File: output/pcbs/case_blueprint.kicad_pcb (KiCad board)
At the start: 2 copper layers, 124.4 x 92.7 mm, 5 parts

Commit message: updated footprints to ceoloide footprints
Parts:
- moved _2 18.7 mm to (183.2, 73.4)
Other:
- net class Default added: clearance 0.2, trace_width 0.25, via_dia 0.8, via_drill 0.4

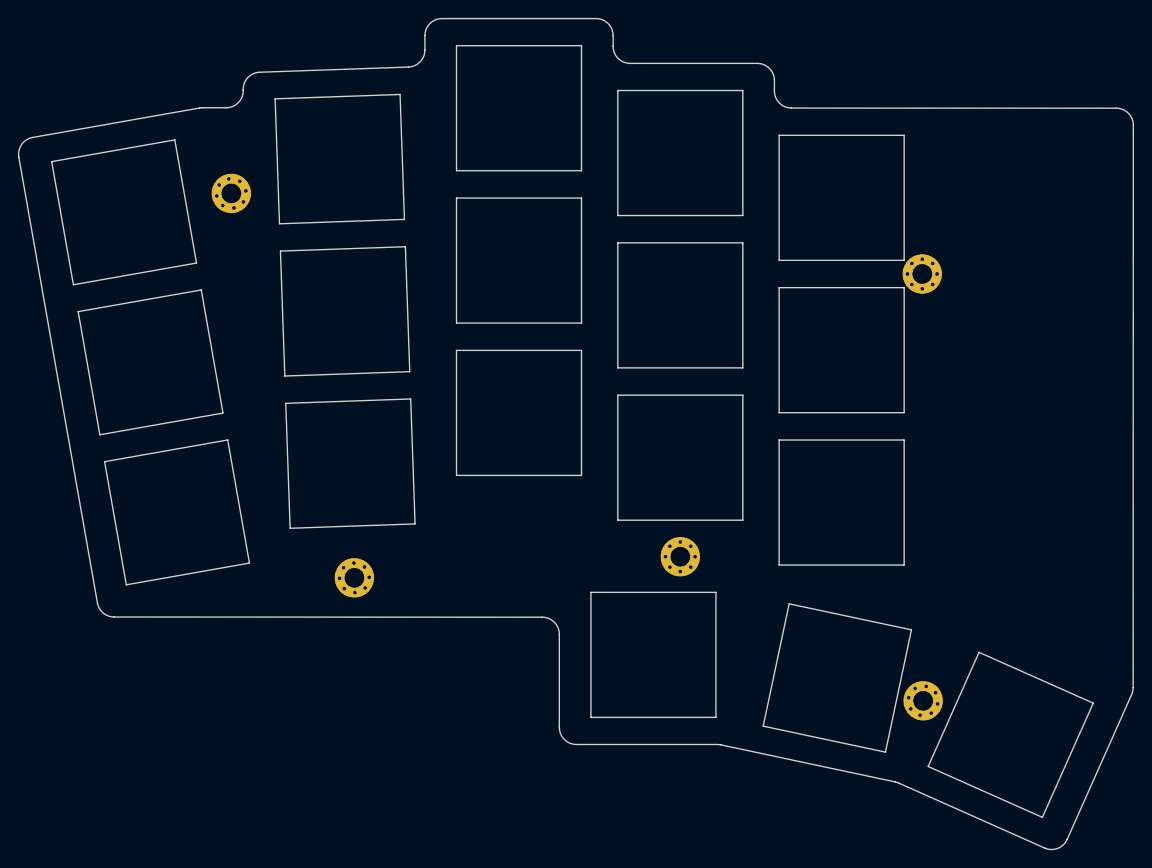
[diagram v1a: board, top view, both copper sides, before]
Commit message: redefined mounting holes positions
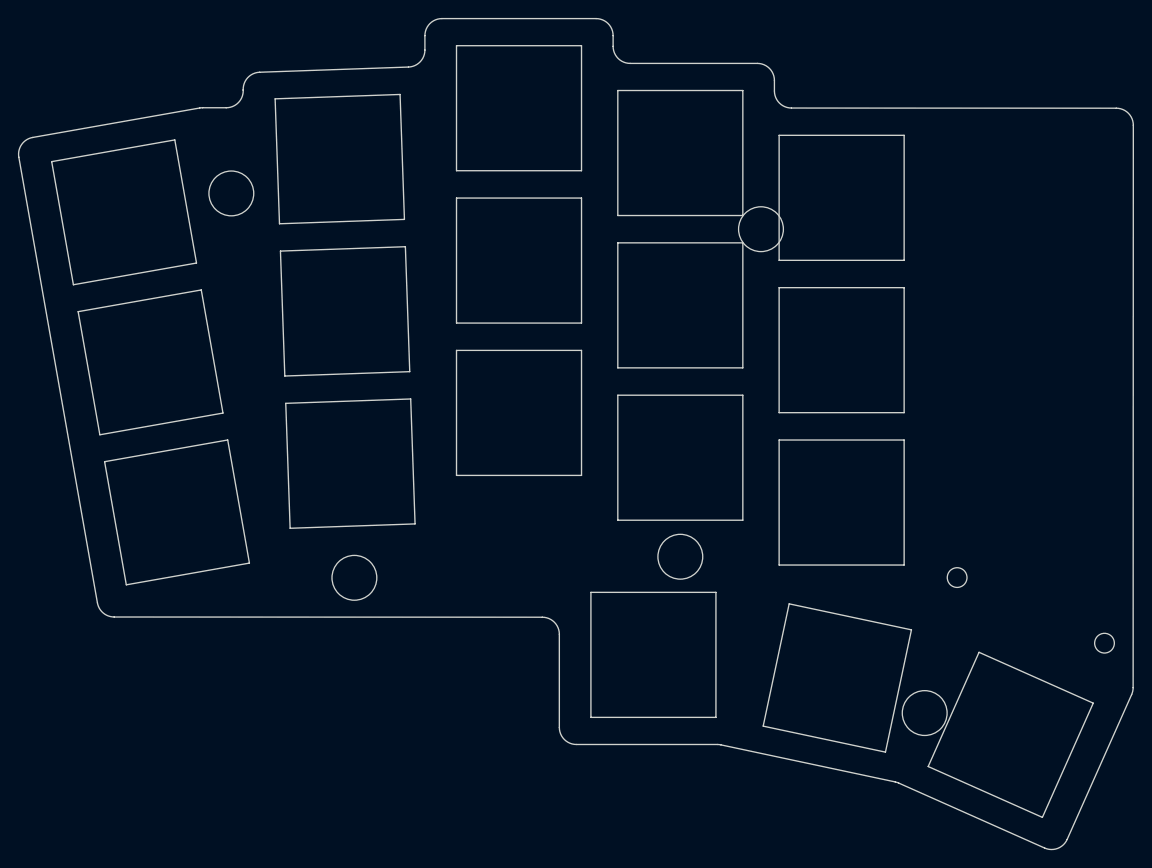
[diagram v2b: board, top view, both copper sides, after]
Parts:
- removed _1, _2, _3, _4, _5: , MountingHole_2.2mm_M2_Pad_Via
- added MH1: , ceoloide:mounting_hole_npth, F.Cu at (203.5, 114.6)
- added MH2: , ceoloide:mounting_hole_npth, F.Cu at (187.1, 107.3)
- added MH3: , ceoloide:mounting_hole_npth, F.Cu at (106.1, 64.4)
- added MH4: , ceoloide:mounting_hole_npth, F.Cu at (165.2, 68.4)
- added MH5: , ceoloide:mounting_hole_npth, F.Cu at (119.8, 107.3)
- added MH6: , ceoloide:mounting_hole_npth, F.Cu at (156.2, 104.9)
- added MH7: , ceoloide:mounting_hole_npth, F.Cu at (183.4, 122.4)
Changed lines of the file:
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@@
     (add_net "")
   )
-    (module "MountingHole_2.2mm_M2_Pad_Via" (version 20210722) (generator pcbnew) (layer "F.Cu")
-      (at 106.06137619999998 64.406711 10)
-      (fp_text reference "_1" (at 0 -3.2) (layer "F.SilkS") hide
-        (effects (font (size 1 1) (thickness 0.15)))
-      )
-      (fp_circle (center 0 0) (end 2.45 0) (layer "F.CrtYd") (width 0.05) (fill none))
-      (pad "1" thru_hole circle locked (at 1.166726 1.166726) (size 0.7 0.7) (drill 0.4) (layers *.Cu *.Mask))
-      (pad "1" thru_hole circle locked (at 0 0) (size 4.4 4.4) (drill 2.2) (layers *.Cu *.Mask))
-      (pad "1" thru_hole circle locked (at 0 1.65) (size 0.7 0.7) (drill 0.4) (layers *.Cu *.Mask))
-      (pad "1" thru_hole circle locked (at 1.166726 -1.166726) (size 0.7 0.7) (drill 0.4) (layers *.Cu *.Mask))
-      (pad "1" thru_hole circle locked (at -1.65 0) (size 0.7 0.7) (drill 0.4) (layers *.Cu *.Mask))
-      (pad "1" thru_hole circle locked (at -1.166726 -1.166726) (size 0.7 0.7) (drill 0.4) (layers *.Cu *.Mask))
-      (pad "1" thru_hole circle locked (at -1.166726 1.166726) (size 0.7 0.7) (drill 0.4) (layers *.Cu *.Mask))
-      (pad "1" thru_hole circle locked (at 1.65 0) (size 0.7 0.7) (drill 0.4) (layers *.Cu *.Mask))
-      (pad "1" thru_hole circle locked (at 0 -1.65) (size 0.7 0.7) (drill 0.4) (layers *.Cu *.Mask))
+  (footprint "ceoloide:mounting_hole_npth"
+    (layer "F.Cu")
+    (at 203.49527039999998 114.5930025 -24)
+    (property "Reference" "MH1"
+      (at 0 2.55 -24)
+      (layer "F.SilkS")
+      hide
+      (effects (font (size 1 1) (thickness 0.15)))
     )
-    (module "MountingHole_2.2mm_M2_Pad_Via" (version 20210722) (generator pcbnew) (layer "F.Cu")
-      (at 183.16278699999998 73.3973763 0)
-      (fp_text reference "_2" (at 0 -3.2) (layer "F.SilkS") hide
-        (effects (font (size 1 1) (thickness 0.15)))
-      )
-      (fp_circle (center 0 0) (end 2.45 0) (layer "F.CrtYd") (width 0.05) (fill none))
-      (pad "1" thru_hole circle locked (at 1.166726 1.166726) (size 0.7 0.7) (drill 0.4) (layers *.Cu *.Mask))
-      (pad "1" thru_hole circle locked (at 0 0) (size 4.4 4.4) (drill 2.2) (layers *.Cu *.Mask))
-      (pad "1" thru_hole circle locked (at 0 1.65) (size 0.7 0.7) (drill 0.4) (layers *.Cu *.Mask))
-      (pad "1" thru_hole circle locked (at 1.166726 -1.166726) (size 0.7 0.7) (drill 0.4) (layers *.Cu *.Mask))
-      (pad "1" thru_hole circle locked (at -1.65 0) (size 0.7 0.7) (drill 0.4) (layers *.Cu *.Mask))
-      (pad "1" thru_hole circle locked (at -1.166726 -1.166726) (size 0.7 0.7) (drill 0.4) (layers *.Cu *.Mask))
-      (pad "1" thru_hole circle locked (at -1.166726 1.166726) (size 0.7 0.7) (drill 0.4) (layers *.Cu *.Mask))
-      (pad "1" thru_hole circle locked (at 1.65 0) (size 0.7 0.7) (drill 0.4) (layers *.Cu *.Mask))
-      (pad "1" thru_hole circle locked (at 0 -1.65) (size 0.7 0.7) (drill 0.4) (layers *.Cu *.Mask))
+    (pad "" np_thru_hole circle
+      (at 0 0 -24)
+      (size 2.2 2.2)
+      (drill 2.2)
+      (layers "*.Cu" "*.Mask")
     )
-    (module "MountingHole_2.2mm_M2_Pad_Via" (version 20210722) (generator pcbnew) (layer "F.Cu")
-      (at 119.79382729999999 107.2996539 2)
-      (fp_text reference "_3" (at 0 -3.2) (layer "F.SilkS") hide
-        (effects (font (size 1 1) (thickness 0.15)))
-      )
-      (fp_circle (center 0 0) (end 2.45 0) (layer "F.CrtYd") (width 0.05) (fill none))
-      (pad "1" thru_hole circle locked (at 1.166726 1.166726) (size 0.7 0.7) (drill 0.4) (layers *.Cu *.Mask))
-      (pad "1" thru_hole circle locked (at 0 0) (size 4.4 4.4) (drill 2.2) (layers *.Cu *.Mask))
-      (pad "1" thru_hole circle locked (at 0 1.65) (size 0.7 0.7) (drill 0.4) (layers *.Cu *.Mask))
-      (pad "1" thru_hole circle locked (at 1.166726 -1.166726) (size 0.7 0.7) (drill 0.4) (layers *.Cu *.Mask))
-      (pad "1" thru_hole circle locked (at -1.65 0) (size 0.7 0.7) (drill 0.4) (layers *.Cu *.Mask))
-      (pad "1" thru_hole circle locked (at -1.166726 -1.166726) (size 0.7 0.7) (drill 0.4) (layers *.Cu *.Mask))
-      (pad "1" thru_hole circle locked (at -1.166726 1.166726) (size 0.7 0.7) (drill 0.4) (layers *.Cu *.Mask))
-      (pad "1" thru_hole circle locked (at 1.65 0) (size 0.7 0.7) (drill 0.4) (layers *.Cu *.Mask))
-      (pad "1" thru_hole circle locked (at 0 -1.65) (size 0.7 0.7) (drill 0.4) (layers *.Cu *.Mask))
+  )
+  (footprint "ceoloide:mounting_hole_npth"
+    (layer "F.Cu")
+    (at 187.05145219999997 107.271743 -24)
+    (property "Reference" "MH2"
+      (at 0 2.55 -24)
+      (layer "F.SilkS")
+      hide
+      (effects (font (size 1 1) (thickness 0.15)))
     )
-    (module "MountingHole_2.2mm_M2_Pad_Via" (version 20210722) (generator pcbnew) (layer "F.Cu")
-      (at 156.1627869 104.9473764 0)
-      (fp_text reference "_4" (at 0 -3.2) (layer "F.SilkS") hide
-        (effects (font (size 1 1) (thickness 0.15)))
-      )
-      (fp_circle (center 0 0) (end 2.45 0) (layer "F.CrtYd") (width 0.05) (fill none))
-      (pad "1" thru_hole circle locked (at 1.166726 1.166726) (size 0.7 0.7) (drill 0.4) (layers *.Cu *.Mask))
-      (pad "1" thru_hole circle locked (at 0 0) (size 4.4 4.4) (drill 2.2) (layers *.Cu *.Mask))
-      (pad "1" thru_hole circle locked (at 0 1.65) (size 0.7 0.7) (drill 0.4) (layers *.Cu *.Mask))
-      (pad "1" thru_hole circle locked (at 1.166726 -1.166726) (size 0.7 0.7) (drill 0.4) (layers *.Cu *.Mask))
-      (pad "1" thru_hole circle locked (at -1.65 0) (size 0.7 0.7) (drill 0.4) (layers *.Cu *.Mask))
-      (pad "1" thru_hole circle locked (at -1.166726 -1.166726) (size 0.7 0.7) (drill 0.4) (layers *.Cu *.Mask))
-      (pad "1" thru_hole circle locked (at -1.166726 1.166726) (size 0.7 0.7) (drill 0.4) (layers *.Cu *.Mask))
-      (pad "1" thru_hole circle locked (at 1.65 0) (size 0.7 0.7) (drill 0.4) (layers *.Cu *.Mask))
-      (pad "1" thru_hole circle locked (at 0 -1.65) (size 0.7 0.7) (drill 0.4) (layers *.Cu *.Mask))
+    (pad "" np_thru_hole circle
+      (at 0 0 -24)
+      (size 2.2 2.2)
+      (drill 2.2)
+      (layers "*.Cu" "*.Mask")
     )
-    (module "MountingHole_2.2mm_M2_Pad_Via" (version 20210722) (generator pcbnew) (layer "F.Cu")
-      (at 183.26111179999998 121.0248061 -12)
-      (fp_text reference "_5" (at 0 -3.2) (layer "F.SilkS") hide
-        (effects (font (size 1 1) (thickness 0.15)))
-      )
-      (fp_circle (center 0 0) (end 2.45 0) (layer "F.CrtYd") (width 0.05) (fill none))
-      (pad "1" thru_hole circle locked (at 1.166726 1.166726) (size 0.7 0.7) (drill 0.4) (layers *.Cu *.Mask))
-      (pad "1" thru_hole circle locked (at 0 0) (size 4.4 4.4) (drill 2.2) (layers *.Cu *.Mask))
-      (pad "1" thru_hole circle locked (at 0 1.65) (size 0.7 0.7) (drill 0.4) (layers *.Cu *.Mask))
-      (pad "1" thru_hole circle locked (at 1.166726 -1.166726) (size 0.7 0.7) (drill 0.4) (layers *.Cu *.Mask))
-      (pad "1" thru_hole circle locked (at -1.65 0) (size 0.7 0.7) (drill 0.4) (layers *.Cu *.Mask))
-      (pad "1" thru_hole circle locked (at -1.166726 -1.166726) (size 0.7 0.7) (drill 0.4) (layers *.Cu *.Mask))
-      (pad "1" thru_hole circle locked (at -1.166726 1.166726) (size 0.7 0.7) (drill 0.4) (layers *.Cu *.Mask))
-      (pad "1" thru_hole circle locked (at 1.65 0) (size 0.7 0.7) (drill 0.4) (layers *.Cu *.Mask))
-      (pad "1" thru_hole circle locked (at 0 -1.65) (size 0.7 0.7) (drill 0.4) (layers *.Cu *.Mask))
+  )
+  (footprint "ceoloide:mounting_hole_npth"
+    (layer "F.Cu")
+    (at 106.06137619999998 64.406711 10)
+    (property "Reference" "MH3"
+      (at 0 2.55 10)
+      (layer "F.SilkS")
+      hide
+      (effects (font (size 1 1) (thickness 0.15)))
     )
+    (pad "" np_thru_hole circle
+      (at 0 0 10)
+      (size 5 5)
+      (drill 5)
+      (layers "*.Cu" "*.Mask")
+    )
+  )
+  (footprint "ceoloide:mounting_hole_npth"
+    (layer "F.Cu")
+    (at 165.1627869 68.3973764 0)
+    (property "Reference" "MH4"
+      (at 0 2.55 0)
+      (layer "F.SilkS")
+      hide
+      (effects (font (size 1 1) (thickness 0.15)))
+    )
+    (pad "" np_thru_hole circle
+      (at 0 0 0)
+      (size 5 5)
+      (drill 5)
+      (layers "*.Cu" "*.Mask")
+    )
+  )
+  (footprint "ceoloide:mounting_hole_npth"
+    (layer "F.Cu")
+    (at 119.79382729999999 107.2996539 2)
+    (property "Reference" "MH5"
+      (at 0 2.55 2)
+      (layer "F.SilkS")
+      hide
+      (effects (font (size 1 1) (thickness 0.15)))
+    )
+    (pad "" np_thru_hole circle
+      (at 0 0 2)
+      (size 5 5)
+      (drill 5)
+      (layers "*.Cu" "*.Mask")
+    )
+  )
+  (footprint "ceoloide:mounting_hole_npth"
+    (layer "F.Cu")
+    (at 156.1627869 104.9473764 0)
+    (property "Reference" "MH6"
+      (at 0 2.55 0)
+      (layer "F.SilkS")
+      hide
+      (effects (font (size 1 1) (thickness 0.15)))
+    )
+    (pad "" np_thru_hole circle
+      (at 0 0 0)
+      (size 5 5)
+      (drill 5)
+      (layers "*.Cu" "*.Mask")
+    )
+  )
+  (footprint "ceoloide:mounting_hole_npth"
+    (layer "F.Cu")
+    (at 183.430993 122.3899583 -12)
+    (property "Reference" "MH7"
+      (at 0 2.55 -12)
+      (layer "F.SilkS")
+      hide
+      (effects (font (size 1 1) (thickness 0.15)))
+    )
+    (pad "" np_thru_hole circle
+      (at 0 0 -12)
+      (size 5 5)
+      (drill 5)
+      (layers "*.Cu" "*.Mask")
+    )
+  )
   (gr_line (start 82.34893033616795 60.36289942290733) (end 91.11929746327908 110.10212306543963) (angle 90) (layer Edge.Cuts) (width 0.15))
 (gr_line (start 102.53578472737154 54.87410181202517) (end 83.89013346903909 58.16183317590318) (angle 90) (layer Edge.Cuts) (width 0.15))

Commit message: designed a new plate case for the keyboard
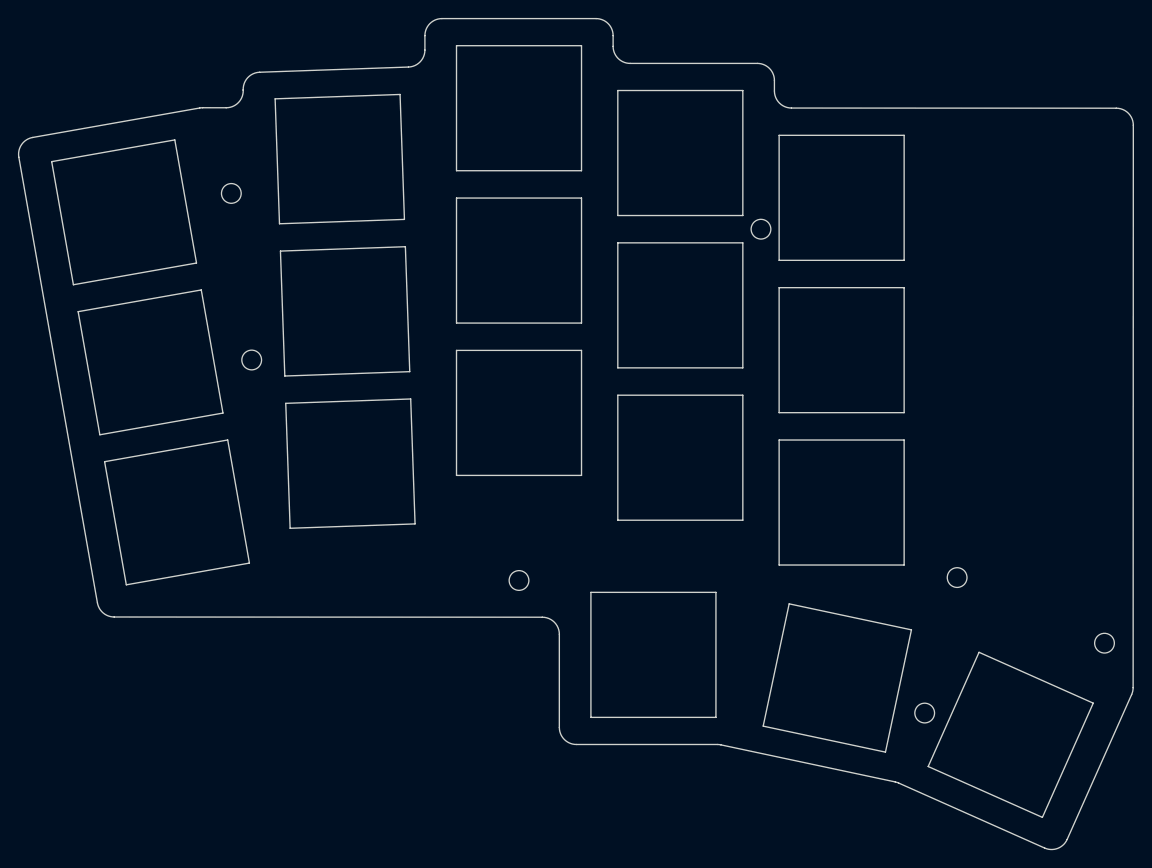
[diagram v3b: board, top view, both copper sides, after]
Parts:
- moved MH5 26.9 mm to (108.3, 83.0), turned to 10 degrees
- moved MH6 18.2 mm to (138.2, 107.6)
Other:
- net class Default removed

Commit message: redesigned the PCB to avoid errors, removed choc v2 support
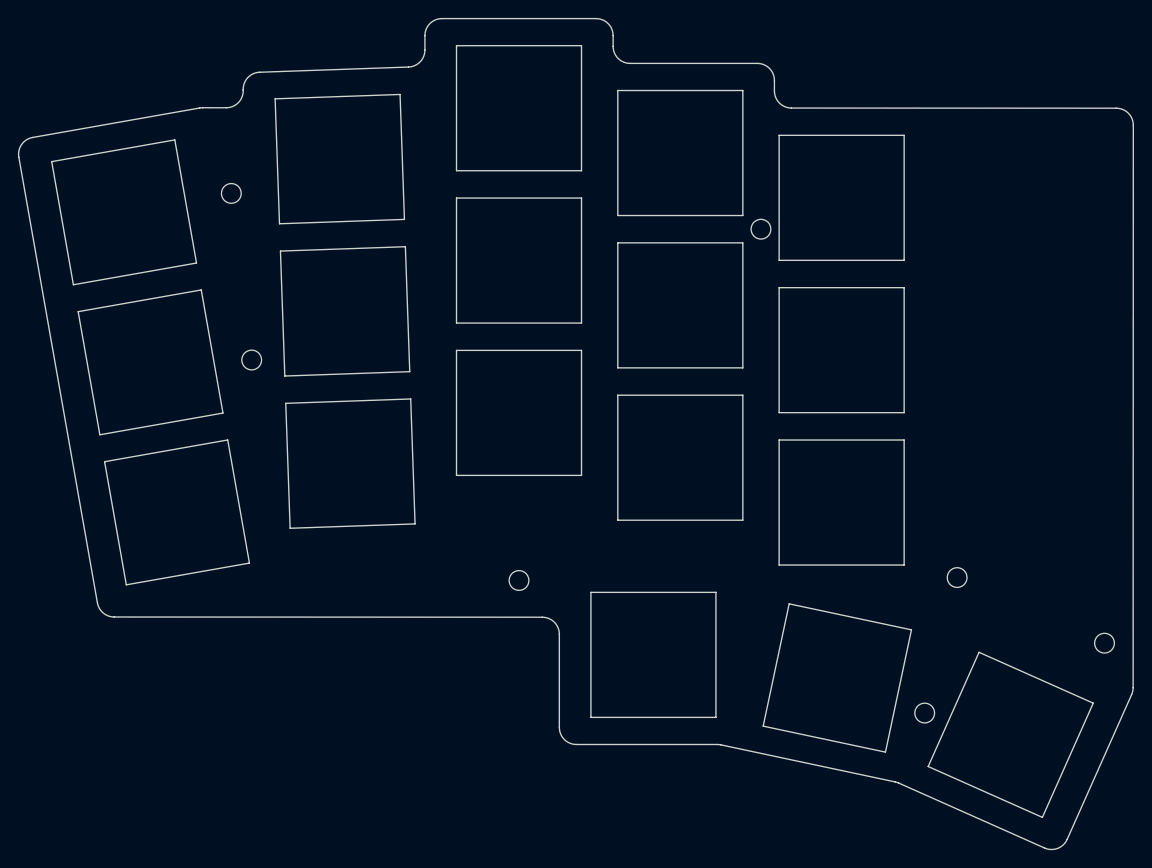
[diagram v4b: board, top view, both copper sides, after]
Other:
- net class Default added: clearance 0.2, trace_width 0.25, via_dia 0.8, via_drill 0.4
